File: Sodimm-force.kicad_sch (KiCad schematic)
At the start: 0 parts

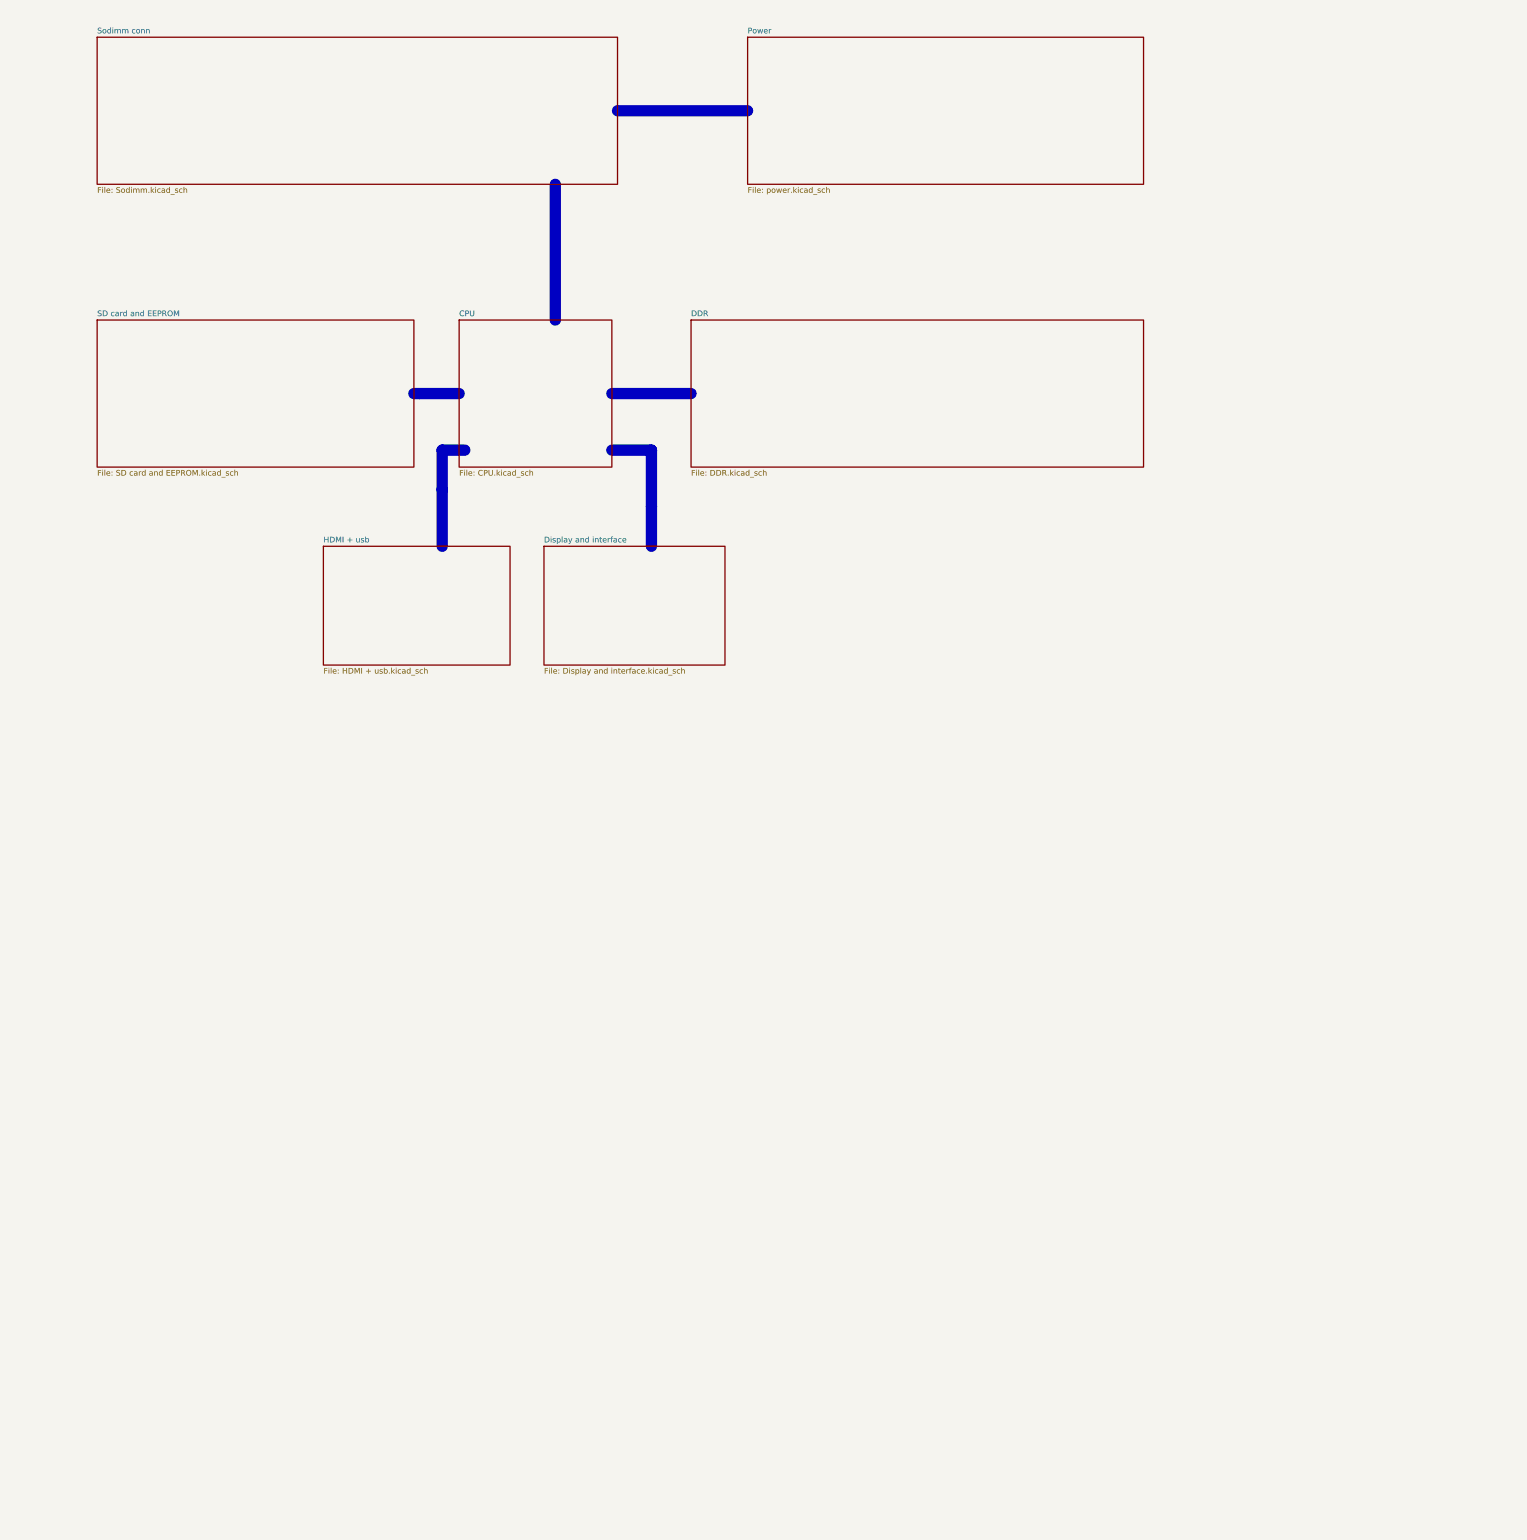
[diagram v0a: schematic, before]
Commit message: расставлены основные блоки и компоненты, подобраны компоненты интерфейса и питания
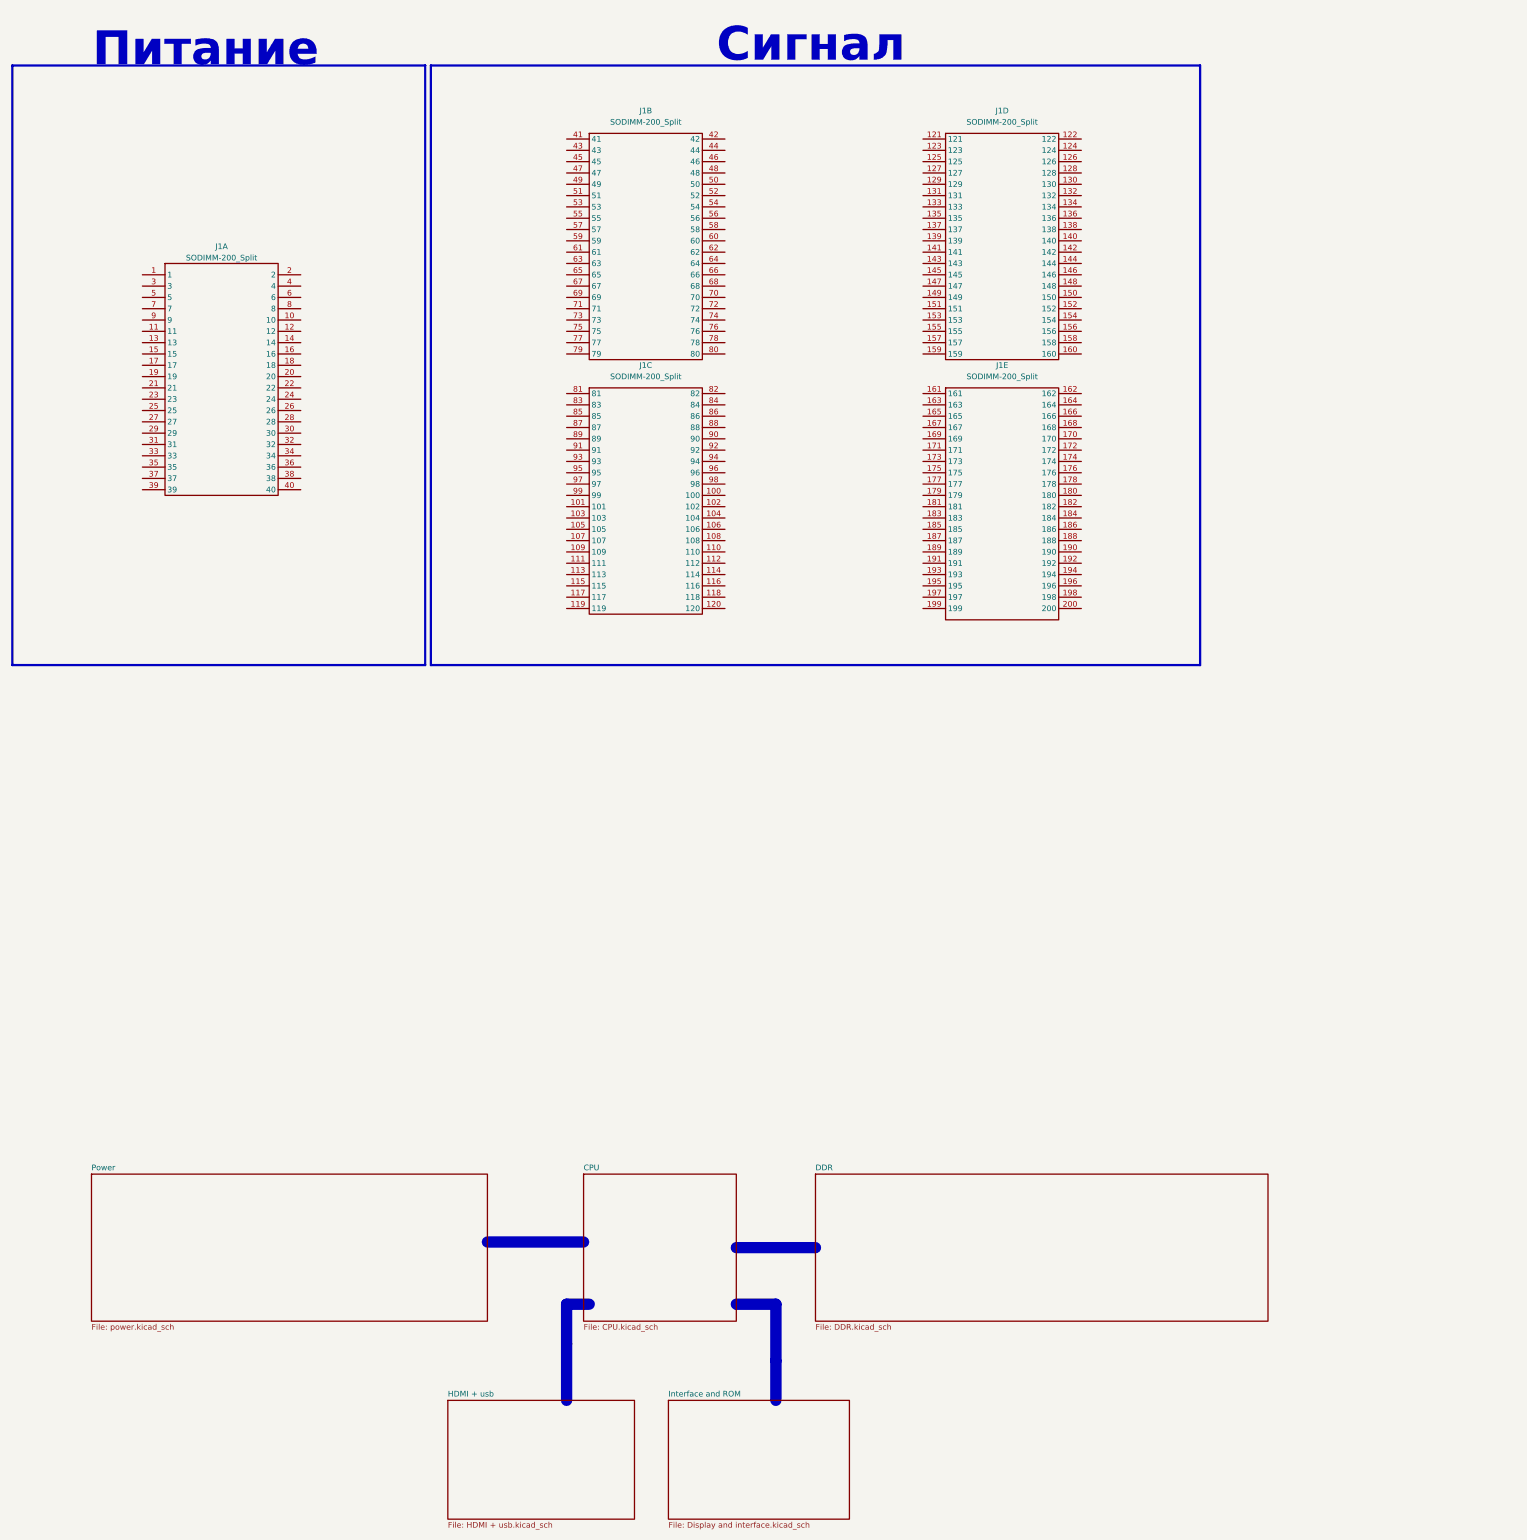
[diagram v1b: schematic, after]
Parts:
- added J1: SODIMM-200_Split, symbol Connector:SODIMM-200_Split
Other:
- sheet Display and interface renamed Interface and ROM
- removed sheet SD card and EEPROM
- removed sheet Sodimm conn
- note added: "Питание"
- note added: "Сигнал"

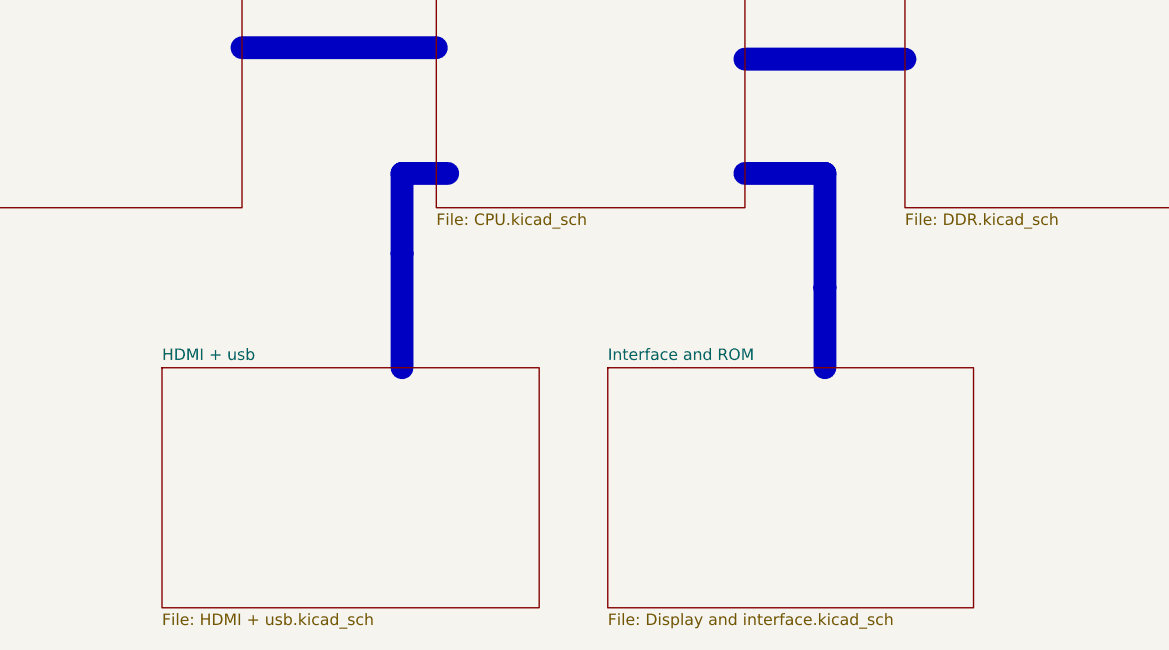
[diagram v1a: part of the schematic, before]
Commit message: Обновлена структура, закончен интерфейс, HDMI Завершено проектирование линий питания и подтяжек для интерфейсов
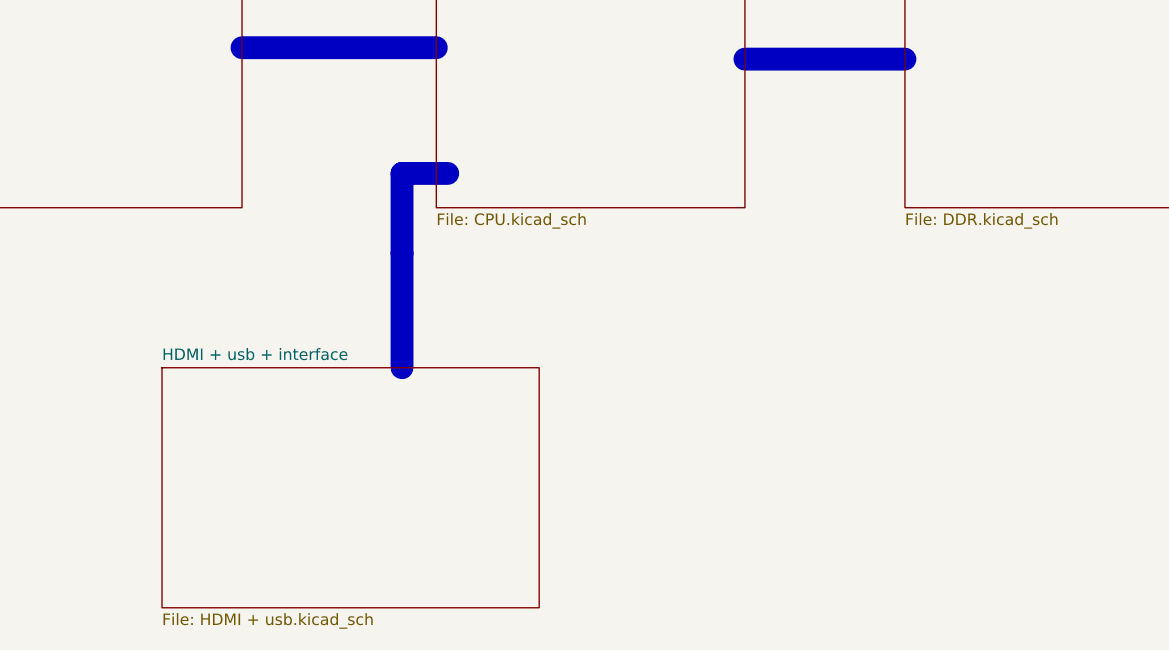
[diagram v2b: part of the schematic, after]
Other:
- sheet HDMI + usb renamed HDMI + usb + interface
- removed sheet Interface and ROM
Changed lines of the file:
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@@
 	(polyline
 		(pts
-			(xy 240.03 351.79) (xy 248.92 351.79)
+			(xy 201.93 373.38) (xy 201.93 360.68)
 		)
 		(stroke
@@
 	(polyline
 		(pts
-			(xy 248.92 373.38) (xy 248.92 364.49)
-		)
-		(stroke
-			(width 2.54)
-			(type default)
-			(color 255 253 3 1)
-		)
-	)
-	(polyline
-		(pts
-			(xy 201.93 373.38) (xy 201.93 360.68)
-		)
-		(stroke
-			(width 2.54)
-			(type default)
-			(color 255 253 3 1)
-		)
-	)
-	(polyline
-		(pts
 			(xy 184.15 337.82) (xy 205.74 337.82)
-		)
-		(stroke
-			(width 2.54)
-			(type default)
-			(color 255 253 3 1)
-		)
-	)
-	(polyline
-		(pts
-			(xy 248.92 364.49) (xy 248.92 351.79)
 		)
 		(stroke
@@
 			(color 184 255 172 1.0000)
 		)
-		(property "Sheetname" "HDMI + usb"
+		(property "Sheetname" "HDMI + usb + interface"
 			(at 175.26 372.6684 0)
 			(effects
@@
 			(project "Sodimm-force"
 				(path "/b3673bfd-24d8-4789-b63c-c3654dc2bb6e"
-					(page "7")
+					(page "5")
 				)
 			)
@@
 			(project "Sodimm-force"
 				(path "/b3673bfd-24d8-4789-b63c-c3654dc2bb6e"
-					(page "4")
+					(page "3")
 				)
 			)
@@
 			(project "Sodimm-force"
 				(path "/b3673bfd-24d8-4789-b63c-c3654dc2bb6e"
-					(page "3")
-				)
-			)
-		)
-	)
-	(sheet
-		(at 224.79 373.38)
-		(size 40.64 26.67)
-		(fields_autoplaced yes)
-		(stroke
-			(width 0.1524)
-			(type solid)
-		)
-		(fill
-			(color 255 135 199 1.0000)
-		)
-		(property "Sheetname" "Interface and ROM"
-			(at 224.79 372.6684 0)
-			(effects
-				(font
-					(size 1.27 1.27)
-				)
-				(justify left bottom)
-			)
-		)
-		(property "Sheetfile" "Display and interface.kicad_sch"
-			(at 224.79 400.6346 0)
-			(effects
-				(font
-					(size 1.27 1.27)
-				)
-				(justify left top)
-			)
-		)
-		(instances
-			(project "Sodimm-force"
-				(path "/b3673bfd-24d8-4789-b63c-c3654dc2bb6e"
-					(page "6")
+					(page "2")
 				)
 			)
@@
 			(project "Sodimm-force"
 				(path "/b3673bfd-24d8-4789-b63c-c3654dc2bb6e"
-					(page "5")
-				)
-			)
+					(page "4")
+				)
+			)

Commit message: Схема закончена, часть компонентов расставлена на плате
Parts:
- J1: footprint (none) -> Connector_PCBEdge:SODIMM-200_2.5V_Card_edge
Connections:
- net Earth: now reaches J1.121
- net Earth: now also J1.10, J1.102, J1.104, J1.105, J1.106, J1.108, J1.109, J1.110, J1.112, J1.114, J1.115, J1.116, J1.117, J1.118, J1.119, J1.12, J1.120, J1.122, J1.123, J1.124, J1.125, J1.126, J1.127, J1.128, J1.129, J1.130, J1.131, J1.132, J1.133, J1.134, J1.135, J1.136, J1.137, J1.138, J1.139, J1.14, J1.140, J1.141, J1.142, J1.143, J1.144, J1.145, J1.146, J1.147, J1.148, J1.149, J1.150, J1.151, J1.152, J1.153, J1.154, J1.155, J1.156, J1.157, J1.158, J1.159, J1.16, J1.160, J1.161, J1.162, J1.163, J1.164, J1.165, J1.166, J1.167, J1.168, J1.169, J1.170, J1.171, J1.172, J1.173, J1.174, J1.175, J1.176, J1.177, J1.178, J1.179, J1.18, J1.180, J1.181, J1.182, J1.183, J1.184, J1.185, J1.186, J1.187, J1.188, J1.189, J1.190, J1.191, J1.192, J1.193, J1.194, J1.195, J1.196, J1.197, J1.198, J1.199, J1.2, J1.20, J1.200, J1.22, J1.24, J1.26, J1.28, J1.30, J1.32, J1.34, J1.36, J1.38, J1.4, J1.40, J1.43, J1.46, J1.49, J1.53, J1.58, J1.6, J1.60, J1.61, J1.62, J1.64, J1.65, J1.66, J1.68, J1.70, J1.71, J1.72, J1.74, J1.76, J1.78, J1.79, J1.8, J1.80, J1.81, J1.82, J1.86, J1.87, J1.90, J1.93, J1.94, J1.98, J1.99
- net LINEOUTL: now reaches J1.100
- net EPHY-TXN: now reaches J1.101
- net EPHY-TXP: now reaches J1.103
- net LRADC: now reaches J1.107
- net PC15: now reaches J1.111
- net PC16: now reaches J1.113
- net USB3-DM: now reaches J1.83
- net PH10/IR_RX: now reaches J1.84
- net USB3-DP: now reaches J1.85
- net PWRON: now reaches J1.88
- net USB2-DM: now reaches J1.89
- net USB2-DP: now reaches J1.91
- net TV-OUT: now reaches J1.92
- net EPHY-RXN: now reaches J1.95
- net LINEOUTR: now reaches J1.96
- net EPHY-RXP: now reaches J1.97
- net VCC-5V: now reaches J1.1
- net VCC-5V: now also J1.11, J1.13, J1.15, J1.3, J1.5, J1.7, J1.9
- net VDD33: now reaches J1.17
- net VDD-CPU: now reaches J1.19
- net VDD-GPU: now reaches J1.21
- net VCC18-ALDO: now reaches J1.23
- net VCC-DRAM: now reaches J1.31
- net VCC33-DLDO: now reaches J1.33
- net PI13: now reaches J1.41
- net SPI1_CS1: now reaches J1.42
- net SPI1_CS0: now reaches J1.44
- net TX5: now reaches J1.45
- net RX5: now reaches J1.47
- net PI3: now reaches J1.48
- net PI4: now reaches J1.50
- net P15: now reaches J1.51
- net PC12: now reaches J1.52
- net PI11: now reaches J1.54
- net SPI1_MOSI: now reaches J1.55
- net PI9: now reaches J1.56
- net SPI1_MISO: now reaches J1.57
- net SPI1_CLK: now reaches J1.59
- net PI12: now reaches J1.63
- net TX0: now reaches J1.67
- net RX0: now reaches J1.69
- net PI1: now reaches J1.73
- net PI14: now reaches J1.75
- net PI6: now reaches J1.77
- no-connect marks 0 -> 6

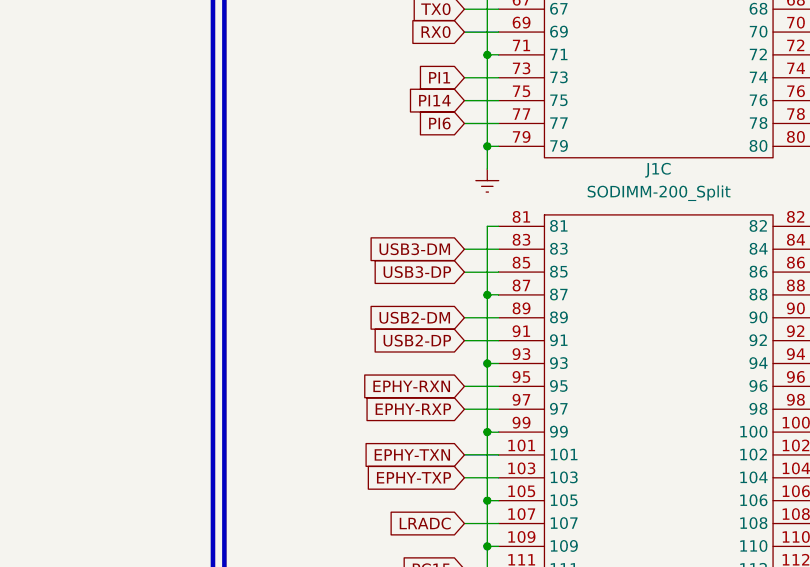
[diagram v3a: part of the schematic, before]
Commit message: Кучка исправлений, переместил SD карту, дисплей, в целом компоновка чуть другая Небольшие исправления в схеме 🤠
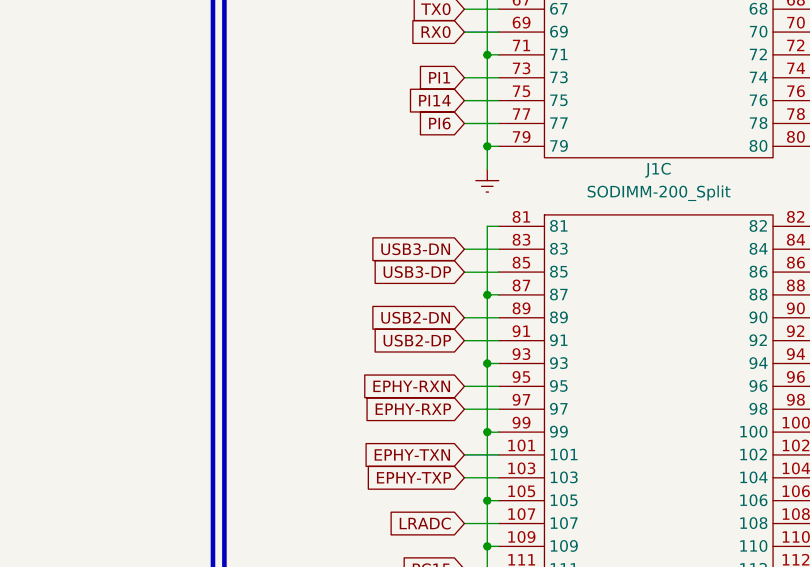
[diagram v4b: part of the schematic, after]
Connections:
- net USB2-DM renamed USB2-DN
- net USB3-DM renamed USB3-DN
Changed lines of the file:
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@@
 (kicad_sch
-	(version 20231120)
+	(version 20250114)
 	(generator "eeschema")
-	(generator_version "8.0")
+	(generator_version "9.0")
 	(paper "A3")
 	(title_block
@@
 		(comment 2 "Корнилов В.В.")
 	)
+	(rectangle
+		(start 77.47 73.66)
+		(end 170.18 208.28)
+		(stroke
+			(width 0.508)
+			(type default)
+			(color 141 151 76 1)
+		)
+		(fill
+			(type none)
+		)
+	)
+	(rectangle
+		(start 171.45 73.66)
+		(end 344.17 208.28)
+		(stroke
+			(width 0.508)
+			(type default)
+			(color 141 151 76 1)
+		)
+		(fill
+			(type none)
+		)
+	)
+	(text "Сигнал"
+		(exclude_from_sim no)
+		(at 256.794 69.088 0)
+		(effects
+			(font
+				(face "GOST type A")
+				(size 7.62 7.62)
+				(thickness 0.254)
+				(bold yes)
+				(color 255 6 0 1)
+			)
+		)
+	)
+	(text "Питание"
+		(exclude_from_sim no)
+		(at 120.904 70.104 0)
+		(effects
+			(font
+				(face "GOST type A")
+				(size 7.62 7.62)
+				(thickness 0.254)
+				(bold yes)
+				(color 255 6 0 1)
+			)
+		)
+	)
 	(junction
 		(at 142.24 153.67)
@@
 		)
 	)
-	(rectangle
-		(start 77.47 73.66)
-		(end 170.18 208.28)
-		(stroke
-			(width 0.508)
-			(type default)
-			(color 141 151 76 1)
-		)
-		(fill
-			(type none)
-		)
-	)
-	(rectangle
-		(start 171.45 73.66)
-		(end 344.17 208.28)
-		(stroke
-			(width 0.508)
-			(type default)
-			(color 141 151 76 1)
-		)
-		(fill
-			(type none)
-		)
-	)
-	(text "Сигнал"
-		(exclude_from_sim no)
-		(at 256.794 69.088 0)
-		(effects
-			(font
-				(face "GOST type A")
-				(size 7.62 7.62)
-				(thickness 0.254)
-				(bold yes)
-				(color 255 6 0 1)
-			)
-		)
-	)
-	(text "Питание"
-		(exclude_from_sim no)
-		(at 120.904 70.104 0)
-		(effects
-			(font
-				(face "GOST type A")
-				(size 7.62 7.62)
-				(thickness 0.254)
-				(bold yes)
-				(color 255 6 0 1)
-			)
-		)
-	)
 	(global_label "PI14"
 		(shape input)
@@
 		)
 	)
-	(global_label "USB3-DM"
+	(global_label "USB3-DN"
 		(shape input)
 		(at 198.12 149.86 180)
@@
 		)
 		(property "Intersheetrefs" "${INTERSHEET_REFS}"
-			(at 193.5358 149.86 0)
+			(at 190.0679 149.86 0)
 			(effects
 				(font
@@
 		)
 	)
-	(global_label "USB2-DM"
+	(global_label "USB2-DN"
 		(shape input)
 		(at 198.12 157.48 180)
@@
 		)
 		(property "Intersheetrefs" "${INTERSHEET_REFS}"
-			(at 193.5358 157.48 0)
+			(at 189.9811 157.48 0)
 			(effects
 				(font
@@
 		(at 175.26 373.38)
 		(size 41.91 26.67)
+		(exclude_from_sim no)
+		(in_bom yes)
+		(on_board yes)
+		(dnp no)
 		(fields_autoplaced yes)
 		(stroke
@@
 		(at 205.74 322.58)
 		(size 34.29 33.02)
+		(exclude_from_sim no)
+		(in_bom yes)
+		(on_board yes)
+		(dnp no)
 		(fields_autoplaced yes)
 		(stroke
@@
 		(at 95.25 322.58)
 		(size 88.9 33.02)
+		(exclude_from_sim no)
+		(in_bom yes)
+		(on_board yes)
+		(dnp no)
 		(fields_autoplaced yes)
 		(stroke
@@
 		(at 257.81 322.58)
 		(size 101.6 33.02)
+		(exclude_from_sim no)
+		(in_bom yes)
+		(on_board yes)
+		(dnp no)
 		(fields_autoplaced yes)
 		(stroke
@@
 		)
 	)
+	(embedded_fonts no)
 )
